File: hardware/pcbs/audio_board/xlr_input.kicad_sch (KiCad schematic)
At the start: 24 parts, among them J1 NC3FAH1, Q1 2N7002, Q2 SI2309CDS-T1-GE3

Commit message: fix libraries
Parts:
- J6: renamed from J1; footprint Library:Jack_XLR_Neutrik_NC3FAH2-LR-DAE_Horizontal -> conn:Jack_XLR_Neutrik_NC3FAH2-LR-DAE_Horizontal
- renumbered C23 to C36, C24 to C37, C25 to C38, C26 to C39, C27 to C40, C28 to C41, D1 to D4, L1 to L4, L2 to L5, Q1 to Q2, Q2 to Q3, R3 to R17, R4 to R18, R5 to R19, R7 to R20, R8 to R21, R9 to R22, R10 to R23, R15 to R24, R16 to R25, R17 to R26, R18 to R27, R19 to R28

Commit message: some more routing
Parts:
- renumbered R17 to R18, R18 to R19, R19 to R20, R20 to R21, R21 to R22, R22 to R23, R23 to R24, R24 to R25, R25 to R26, R26 to R27, R27 to R28, R28 to R29

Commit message: route some more
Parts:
- renumbered C36 to C37, C37 to C38, C38 to C39, C39 to C40, C40 to C41, C41 to C42
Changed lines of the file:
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@@
 		(on_board yes)
 		(dnp no)
-		(property "Reference" "C38"
+		(property "Reference" "C39"
 			(at 85.09 86.36 0)
 			(effects
@@
 			(project "audio_board"
 				(path "/54443f96-c7c5-4432-b890-45b14a1547a1/8957bb4e-7be5-4513-a482-a60a2150a7cb"
-					(reference "C50")
-					(unit 1)
-				)
-				(path "/54443f96-c7c5-4432-b890-45b14a1547a1/91e2e940-fc71-4db8-9476-c8ec62bf0617"
-					(reference "C44")
-					(unit 1)
-				)
-				(path "/54443f96-c7c5-4432-b890-45b14a1547a1/b0f2da11-13c7-4314-8470-ff6d99797a55"
-					(reference "C38")
+					(reference "C51")
+					(unit 1)
+				)
+				(path "/54443f96-c7c5-4432-b890-45b14a1547a1/91e2e940-fc71-4db8-9476-c8ec62bf0617"
+					(reference "C45")
+					(unit 1)
+				)
+				(path "/54443f96-c7c5-4432-b890-45b14a1547a1/b0f2da11-13c7-4314-8470-ff6d99797a55"
+					(reference "C39")
 					(unit 1)
 				)
@@
 		(on_board yes)
 		(dnp no)
-		(property "Reference" "C40"
+		(property "Reference" "C41"
 			(at 162.56 99.06 90)
 			(effects
@@
 			(project "audio_board"
 				(path "/54443f96-c7c5-4432-b890-45b14a1547a1/8957bb4e-7be5-4513-a482-a60a2150a7cb"
-					(reference "C52")
-					(unit 1)
-				)
-				(path "/54443f96-c7c5-4432-b890-45b14a1547a1/91e2e940-fc71-4db8-9476-c8ec62bf0617"
-					(reference "C46")
-					(unit 1)
-				)
-				(path "/54443f96-c7c5-4432-b890-45b14a1547a1/b0f2da11-13c7-4314-8470-ff6d99797a55"
-					(reference "C40")
+					(reference "C53")
+					(unit 1)
+				)
+				(path "/54443f96-c7c5-4432-b890-45b14a1547a1/91e2e940-fc71-4db8-9476-c8ec62bf0617"
+					(reference "C47")
+					(unit 1)
+				)
+				(path "/54443f96-c7c5-4432-b890-45b14a1547a1/b0f2da11-13c7-4314-8470-ff6d99797a55"
+					(reference "C41")
 					(unit 1)
 				)
@@
 		(on_board yes)
 		(dnp no)
-		(property "Reference" "C37"
+		(property "Reference" "C38"
 			(at 78.74 115.57 0)
 			(effects
@@
 			(project "audio_board"
 				(path "/54443f96-c7c5-4432-b890-45b14a1547a1/8957bb4e-7be5-4513-a482-a60a2150a7cb"
-					(reference "C49")
-					(unit 1)
-				)
-				(path "/54443f96-c7c5-4432-b890-45b14a1547a1/91e2e940-fc71-4db8-9476-c8ec62bf0617"
-					(reference "C43")
-					(unit 1)
-				)
-				(path "/54443f96-c7c5-4432-b890-45b14a1547a1/b0f2da11-13c7-4314-8470-ff6d99797a55"
-					(reference "C37")
+					(reference "C50")
+					(unit 1)
+				)
+				(path "/54443f96-c7c5-4432-b890-45b14a1547a1/91e2e940-fc71-4db8-9476-c8ec62bf0617"
+					(reference "C44")
+					(unit 1)
+				)
+				(path "/54443f96-c7c5-4432-b890-45b14a1547a1/b0f2da11-13c7-4314-8470-ff6d99797a55"
+					(reference "C38")
 					(unit 1)
 				)
@@
 		(on_board yes)
 		(dnp no)
-		(property "Reference" "C39"
+		(property "Reference" "C40"
 			(at 157.48 113.0235 0)
 			(effects
@@
 			(project "audio_board"
 				(path "/54443f96-c7c5-4432-b890-45b14a1547a1/8957bb4e-7be5-4513-a482-a60a2150a7cb"
-					(reference "C51")
-					(unit 1)
-				)
-				(path "/54443f96-c7c5-4432-b890-45b14a1547a1/91e2e940-fc71-4db8-9476-c8ec62bf0617"
-					(reference "C45")
-					(unit 1)
-				)
-				(path "/54443f96-c7c5-4432-b890-45b14a1547a1/b0f2da11-13c7-4314-8470-ff6d99797a55"
-					(reference "C39")
+					(reference "C52")
+					(unit 1)
+				)
+				(path "/54443f96-c7c5-4432-b890-45b14a1547a1/91e2e940-fc71-4db8-9476-c8ec62bf0617"
+					(reference "C46")
+					(unit 1)
+				)
+				(path "/54443f96-c7c5-4432-b890-45b14a1547a1/b0f2da11-13c7-4314-8470-ff6d99797a55"
+					(reference "C40")
 					(unit 1)
 				)
@@
 		(on_board yes)
 		(dnp no)
-		(property "Reference" "C41"
+		(property "Reference" "C42"
 			(at 162.56 127 90)
 			(effects
@@
 			(project "audio_board"
 				(path "/54443f96-c7c5-4432-b890-45b14a1547a1/8957bb4e-7be5-4513-a482-a60a2150a7cb"
-					(reference "C53")
-					(unit 1)
-				)
-				(path "/54443f96-c7c5-4432-b890-45b14a1547a1/91e2e940-fc71-4db8-9476-c8ec62bf0617"
-					(reference "C47")
-					(unit 1)
-				)
-				(path "/54443f96-c7c5-4432-b890-45b14a1547a1/b0f2da11-13c7-4314-8470-ff6d99797a55"
-					(reference "C41")
+					(reference "C54")
+					(unit 1)
+				)
+				(path "/54443f96-c7c5-4432-b890-45b14a1547a1/91e2e940-fc71-4db8-9476-c8ec62bf0617"
+					(reference "C48")
+					(unit 1)
+				)
+				(path "/54443f96-c7c5-4432-b890-45b14a1547a1/b0f2da11-13c7-4314-8470-ff6d99797a55"
+					(reference "C42")
 					(unit 1)
 				)
@@
 		(on_board yes)
 		(dnp no)
-		(property "Reference" "C36"
+		(property "Reference" "C37"
 			(at 78.74 107.95 0)
 			(effects
@@
 			(project "audio_board"
 				(path "/54443f96-c7c5-4432-b890-45b14a1547a1/8957bb4e-7be5-4513-a482-a60a2150a7cb"
-					(reference "C48")
-					(unit 1)
-				)
-				(path "/54443f96-c7c5-4432-b890-45b14a1547a1/91e2e940-fc71-4db8-9476-c8ec62bf0617"
-					(reference "C42")
-					(unit 1)
-				)
-				(path "/54443f96-c7c5-4432-b890-45b14a1547a1/b0f2da11-13c7-4314-8470-ff6d99797a55"
-					(reference "C36")
-					(unit 1)
-				)
+					(reference "C49")
+					(unit 1)
+				)
+				(path "/54443f96-c7c5-4432-b890-45b14a1547a1/91e2e940-fc71-4db8-9476-c8ec62bf0617"
+					(reference "C43")
+					(unit 1)
+				)
+				(path "/54443f96-c7c5-4432-b890-45b14a1547a1/b0f2da11-13c7-4314-8470-ff6d99797a55"
+					(reference "C37")
+					(unit 1)
+				)

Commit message: routing almost complete
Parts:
- renumbered C37 to C39, C38 to C40, C39 to C41, C40 to C42, C41 to C43, C42 to C44

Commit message: finish routing
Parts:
- renumbered R18 to R17, R19 to R18, R20 to R19, R21 to R20, R22 to R21, R23 to R22, R24 to R23, R25 to R24, R26 to R25, R27 to R26, R28 to R27, R29 to R28

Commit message: component values
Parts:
- D4: LCSC C12333 -> (none)
- J6: MPN (none) -> NC3FAH1; Part NC3FAH1 -> (none); Shop https://eu.mouser.com/ProductDetail/Neutrik/NC3FAH1?qs=jCym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 -> (none)
- L4, L5: LCSC C1046 -> (none)
- Q2: LCSC C8545 -> (none); Part 2N7002 -> (none)
- R17: MPN R 10kΩ 125mW 5% 0603 -> (none)
- R18: MPN R 22kΩ 125mW 5% 0603 -> (none)
- R19, R25: MPN R 100kΩ 125mW 5% 0603 -> (none)
- R20, R22: MPN R 6.8kΩ 125mW 1% 0603 -> (none)
- R21: MPN R 470Ω 125mW 5% 0603 -> (none)
- R23, R24: MPN R 2.2kΩ 125mW 1% 0603 -> (none)
- R26: MPN R 13kΩ 125mW 1% 0603 -> (none)
- R27, R28: MPN 1MΩ 125mW 5% 0603 -> (none)
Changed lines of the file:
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@@
 			)
 		)
-		(property "MPN" "R 2.2kΩ 125mW 1% 0603"
+		(property "MPN" ""
 			(at 113.03 123.19 90)
 			(effects
@@
 			)
 		)
-		(property "MPN" "R 2.2kΩ 125mW 1% 0603"
+		(property "MPN" ""
 			(at 113.03 105.41 90)
 			(effects
@@
 			)
 		)
-		(property "MPN" "R 6.8kΩ 125mW 1% 0603"
+		(property "MPN" ""
 			(at 102.87 90.17 0)
 			(effects
@@
 		)
 		(property "MPN" "PRTR5V0U2X,215"
-			(at 201.93 114.3 0)
-			(effects
-				(font
-					(size 1.27 1.27)
-				)
-				(hide yes)
-			)
-		)
-		(property "LCSC" "C12333"
 			(at 201.93 114.3 0)
 			(effects
@@
 			)
 		)
-		(property "MPN" "1MΩ 125mW 5% 0603"
+		(property "MPN" ""
 			(at 179.07 106.68 0)
 			(effects
@@
 			)
 		)
-		(property "LCSC" "C1046"
-			(at 86.36 123.19 90)
-			(effects
-				(font
-					(size 1.27 1.27)
-				)
-				(hide yes)
-			)
-		)
 		(pin "1"
 		)
@@
 			)
 		)
-		(property "Part" "NC3FAH1"
-			(at 45.72 105.41 0)
-			(effects
-				(font
-					(size 1.27 1.27)
-				)
-				(hide yes)
-			)
-		)
-		(property "Shop" "https://eu.mouser.com/ProductDetail/Neutrik/NC3FAH1?qs=jCymNF74TgUeDVE6PPGqug%3D%3D"
+		(property "MPN" "NC3FAH1"
 			(at 45.72 105.41 0)
 			(effects
@@
 			)
 		)
-		(property "MPN" "R 100kΩ 125mW 5% 0603"
+		(property "MPN" ""
 			(at 72.39 54.61 0)
 			(effects
@@
 			)
 		)
-		(property "MPN" "R 6.8kΩ 125mW 1% 0603"
+		(property "MPN" ""
 			(at 97.79 90.17 0)
 			(effects
@@
 			)
 		)
-		(property "Part" "2N7002"
-			(at 69.85 66.04 0)
-			(effects
-				(font
-					(size 1.27 1.27)
-				)
-				(hide yes)
-			)
-		)
-		(property "LCSC" "C8545"
-			(at 69.85 66.04 0)
-			(effects
-				(font
-					(size 1.27 1.27)
-				)
-				(hide yes)
-			)
-		)
 		(property "MPN" "2N7002"
 			(at 69.85 66.04 0)
@@
 		)
 		(property "MPN" "SDFL1608S100KTF or LQM21FN100N00L"
-			(at 87.63 105.41 90)
-			(effects
-				(font
-					(size 1.27 1.27)
-				)
-				(hide yes)
-			)
-		)
-		(property "LCSC" "C1046"
 			(at 87.63 105.41 90)
 			(effects
@@
 			)
 		)
-		(property "MPN" "R 100kΩ 125mW 5% 0603"
+		(property "MPN" ""
 			(at 114.3 90.17 0)
 			(effects
@@
 			)
 		)
-		(property "MPN" "1MΩ 125mW 5% 0603"
+		(property "MPN" ""
 			(at 179.07 121.92 0)
 			(effects
@@
 			)
 		)
-		(property "MPN" "R 22kΩ 125mW 5% 0603"
+		(property "MPN" ""
 			(at 72.39 41.91 0)
 			(effects
@@
 			)
 		)
-		(property "MPN" "R 470Ω 125mW 5% 0603"
+		(property "MPN" ""
 			(at 100.33 60.96 0)
 			(effects
@@
 			)
 		)
-		(property "MPN" "R 13kΩ 125mW 1% 0603"
+		(property "MPN" ""
 			(at 123.19 114.3 0)
 			(effects
@@
 			)
 		)
-		(property "MPN" "R 10kΩ 125mW 5% 0603"
+		(property "MPN" ""
 			(at 60.96 72.39 0)
 			(effects

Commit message: revise BOM
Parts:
- L4, L5: MPN SDFL1608S100KTF or LQM21FN100N00L -> LQM21FN100N00L
- R17: MPN (none) -> R 10kΩ 125mW 1% 0805
- R18: MPN (none) -> R 22kΩ 125mW 1% 0805
- R19, R25: MPN (none) -> R 100kΩ 125mW 1% 0805
- R20, R22: MPN (none) -> R 6.8kΩ 125mW 1% 0805
- R21: MPN (none) -> R 470Ω 125mW 1% 0805
- R23, R24: MPN (none) -> R 2.2kΩ 125mW 1% 0805
- R26: MPN (none) -> R 13kΩ 125mW 1% 0805
- R27, R28: MPN (none) -> R 1MΩ 125mW 1% 0805
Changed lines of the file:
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@@
 			)
 		)
-		(property "MPN" ""
+		(property "MPN" "R 2.2kΩ 125mW 1% 0805"
 			(at 113.03 123.19 90)
 			(effects
@@
 			)
 		)
-		(property "MPN" ""
+		(property "MPN" "R 2.2kΩ 125mW 1% 0805"
 			(at 113.03 105.41 90)
 			(effects
@@
 			)
 		)
-		(property "MPN" ""
+		(property "MPN" "R 6.8kΩ 125mW 1% 0805"
 			(at 102.87 90.17 0)
 			(effects
@@
 			)
 		)
-		(property "MPN" ""
+		(property "MPN" "R 1MΩ 125mW 1% 0805"
 			(at 179.07 106.68 0)
 			(effects
@@
 			)
 		)
-		(property "MPN" "SDFL1608S100KTF or LQM21FN100N00L"
+		(property "MPN" "LQM21FN100N00L"
 			(at 86.36 123.19 90)
 			(effects
@@
 			)
 		)
-		(property "MPN" ""
+		(property "MPN" "R 100kΩ 125mW 1% 0805"
 			(at 72.39 54.61 0)
 			(effects
@@
 			)
 		)
-		(property "MPN" ""
+		(property "MPN" "R 6.8kΩ 125mW 1% 0805"
 			(at 97.79 90.17 0)
 			(effects
@@
 			)
 		)
-		(property "MPN" "SDFL1608S100KTF or LQM21FN100N00L"
+		(property "MPN" "LQM21FN100N00L"
 			(at 87.63 105.41 90)
 			(effects
@@
 			)
 		)
-		(property "MPN" ""
+		(property "MPN" "R 100kΩ 125mW 1% 0805"
 			(at 114.3 90.17 0)
 			(effects
@@
 			)
 		)
-		(property "MPN" ""
+		(property "MPN" "R 1MΩ 125mW 1% 0805"
 			(at 179.07 121.92 0)
 			(effects
@@
 			)
 		)
-		(property "MPN" ""
+		(property "MPN" "R 22kΩ 125mW 1% 0805"
 			(at 72.39 41.91 0)
 			(effects
@@
 			)
 		)
-		(property "MPN" ""
+		(property "MPN" "R 470Ω 125mW 1% 0805"
 			(at 100.33 60.96 0)
 			(effects
@@
 			)
 		)
-		(property "MPN" ""
+		(property "MPN" "R 13kΩ 125mW 1% 0805"
 			(at 123.19 114.3 0)
 			(effects
@@
 			)
 		)
-		(property "MPN" ""
+		(property "MPN" "R 10kΩ 125mW 1% 0805"
 			(at 60.96 72.39 0)
 			(effects

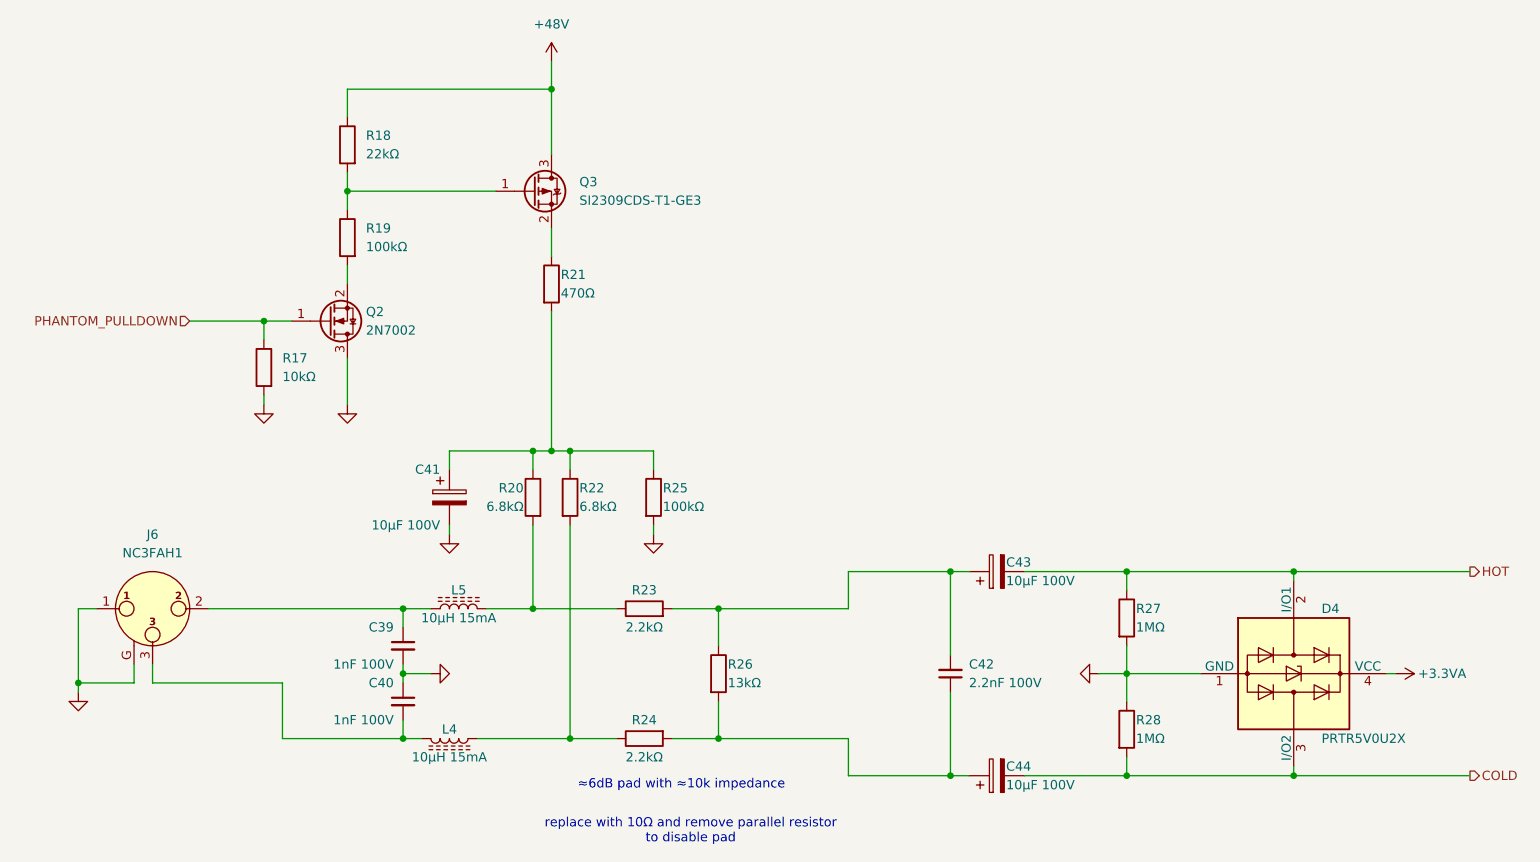
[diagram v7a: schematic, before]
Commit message: slew rate limiting resistors
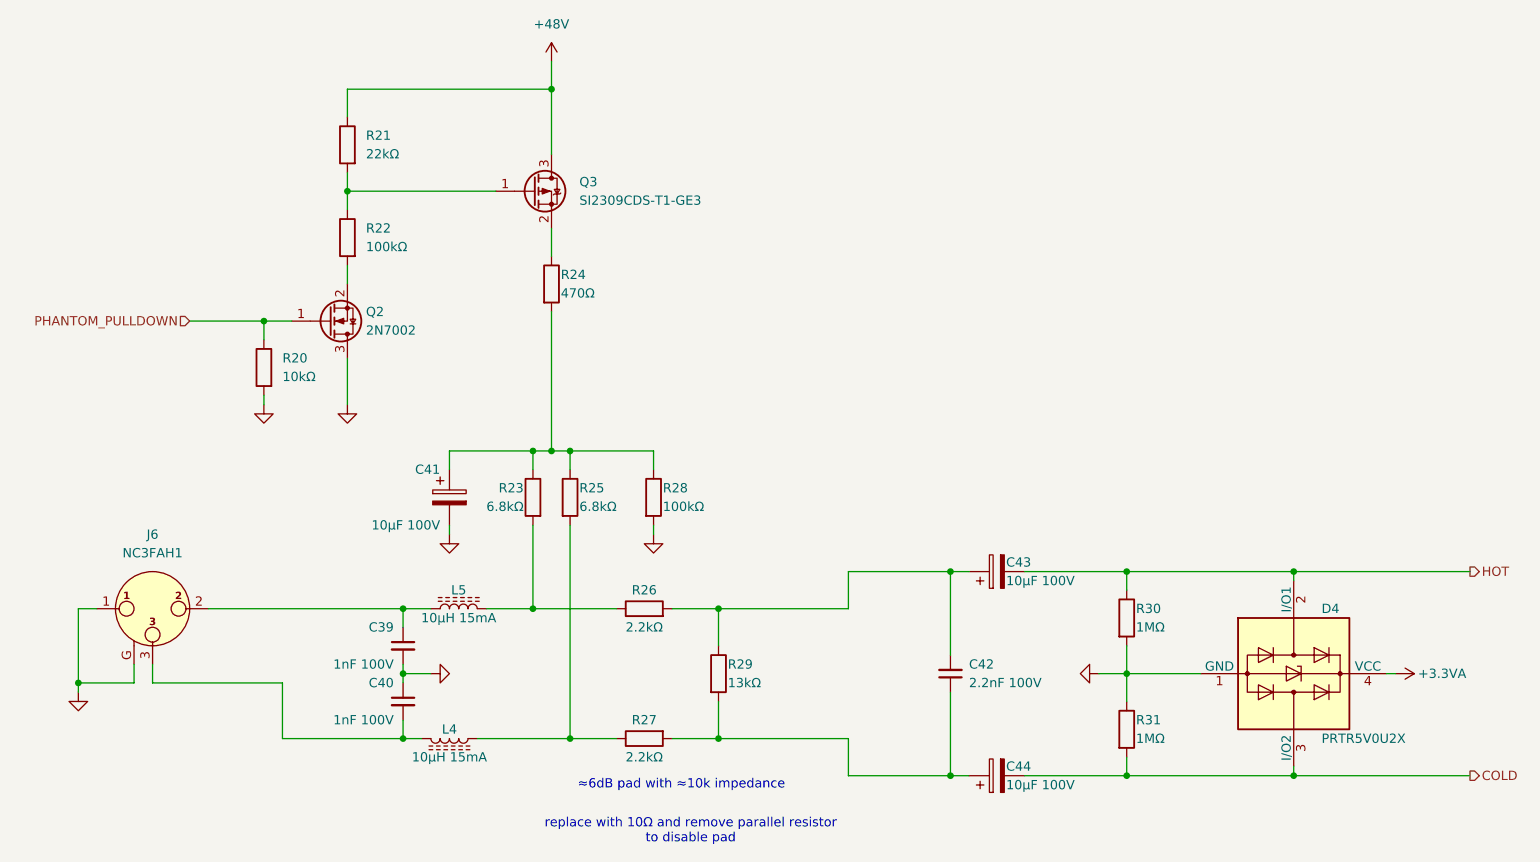
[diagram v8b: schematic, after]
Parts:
- renumbered R17 to R20, R18 to R21, R19 to R22, R20 to R23, R21 to R24, R22 to R25, R23 to R26, R24 to R27, R25 to R28, R26 to R29, R27 to R30, R28 to R31
